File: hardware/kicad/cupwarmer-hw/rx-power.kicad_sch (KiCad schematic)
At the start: 41 parts, among them J1 I2C Service, J3 STATUS_MON, U1 STWLC38JRM

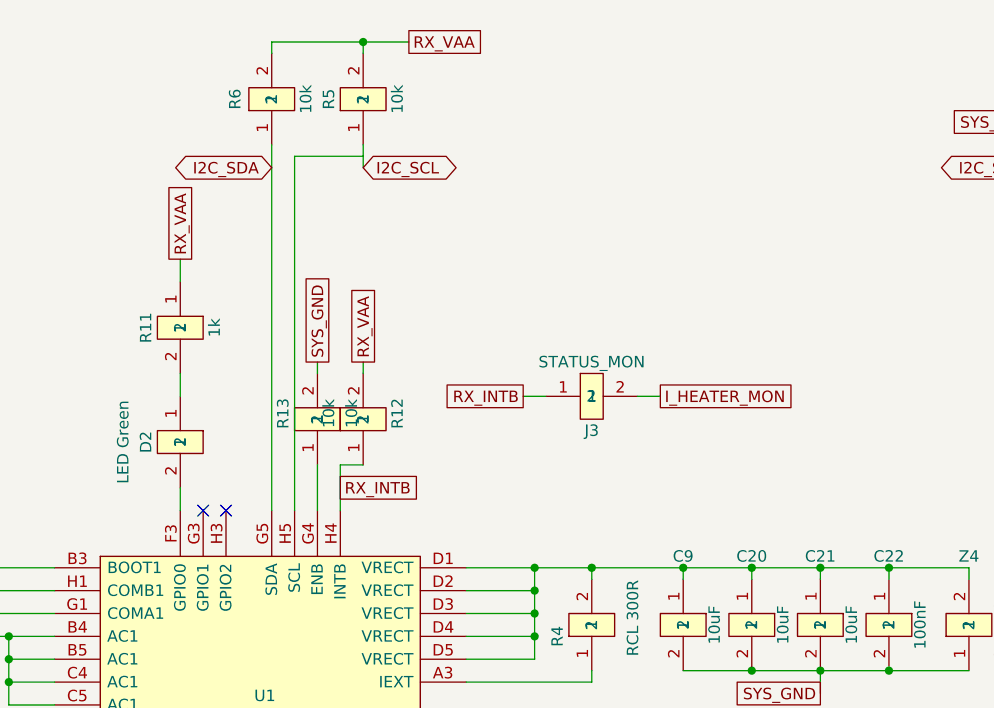
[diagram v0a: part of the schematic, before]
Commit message: Drop Cd (C15) parallel resonant cap
UM3154 §9.1.2 documents Cd as optional, used only for Qi-cert
backward compatibility with specific TX coils. cupwarmer is not
pursuing Qi certification, so the cap adds drift and loss without
benefit. Removed C15 (3.3 nF NP0 / Walsin 0603N332J500CT) from
the rx-power schematic, the PCB, and the BOM. Decision recorded
in docs/design-notes.md.

ERC clean; sch↔board parity unchanged otherwise.
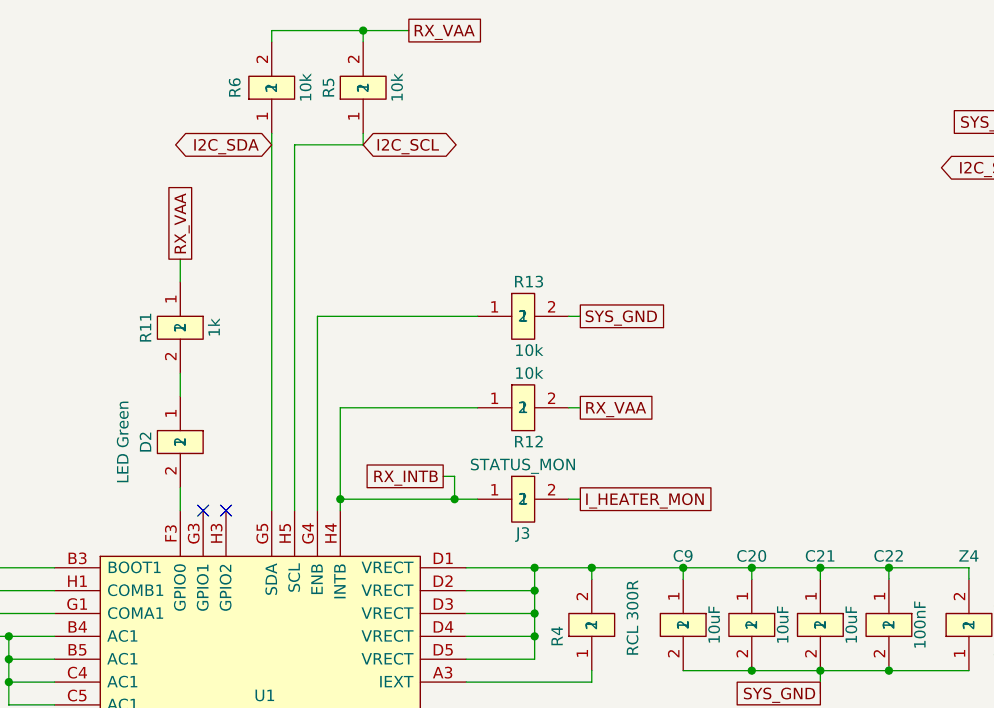
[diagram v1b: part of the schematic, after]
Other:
- moved on the sheet: J3, R12, R13, R5, R6

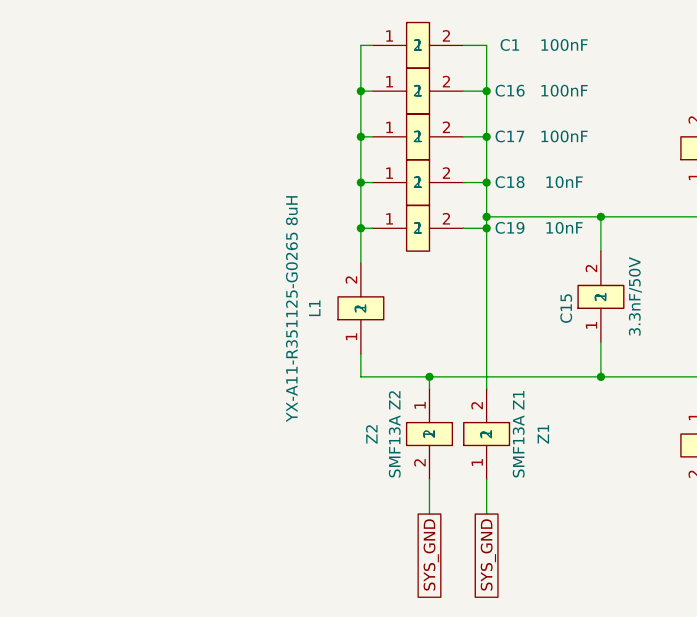
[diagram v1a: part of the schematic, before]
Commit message: Switch L1 footprint to Würth 760308102207 (P5.0mm)
Custom SolderWire footprint with 5.0mm pitch and φ1.2mm holes
matching the WE-WPCC 760308102207 lead pattern. Includes a
40×40mm rounded-square outline on Dwgs.User as a placement guide
for the coil module body. Schematic L1 properties (Value, MPN,
Manufacturer, LCSC, Footprint) updated to match the BOM.

ERC clean; PCB parity unchanged; no new DRC violations on L1.
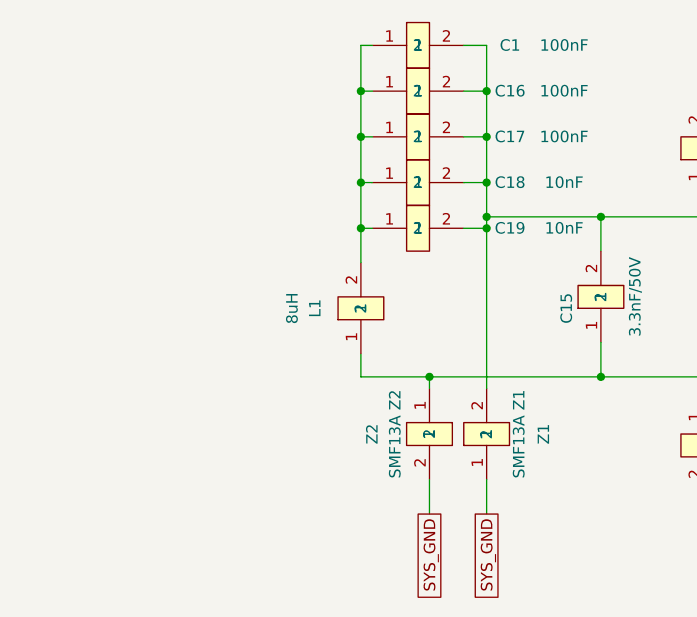
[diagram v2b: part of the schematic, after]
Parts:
- L1: value YX-A11-R351125-G0265 8uH -> 8uH; footprint Connector_Wire:SolderWire-0.5sqmm_1x02_P4.8mm_D0.9mm_OD2.3mm -> cupwarmer:SolderWire-Wuerth760308_1x02_P5.0mm_D1.2mm; LCSC C49297385 -> (none); MPN YX-A11-R351125-G0265 -> 760308102207; Manufacturer CND-tek -> Wuerth Elektronik
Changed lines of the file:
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@@
 			)
 		)
-		(property "Value" "YX-A11-R351125-G0265 8uH"
+		(property "Value" "8uH"
 			(at 50.8 105.41 0)
 			(show_name no)
@@
 			)
 		)
-		(property "Footprint" "Connector_Wire:SolderWire-0.5sqmm_1x02_P4.8mm_D0.9mm_OD2.3mm"
+		(property "Footprint" "cupwarmer:SolderWire-Wuerth760308_1x02_P5.0mm_D1.2mm"
 			(at 58.42 105.41 0)
 			(hide yes)
@@
 			)
 		)
-		(property "Manufacturer" "CND-tek"
+		(property "Manufacturer" "Wuerth Elektronik"
 			(at 0 0 0)
 			(hide yes)
@@
 			)
 		)
-		(property "LCSC" "C49297385"
+		(property "LCSC" ""
 			(at 0 0 0)
 			(hide yes)
@@
 			)
 		)
-		(property "MPN" "YX-A11-R351125-G0265"
+		(property "MPN" "760308102207"
 			(at 0 0 0)
 			(hide yes)

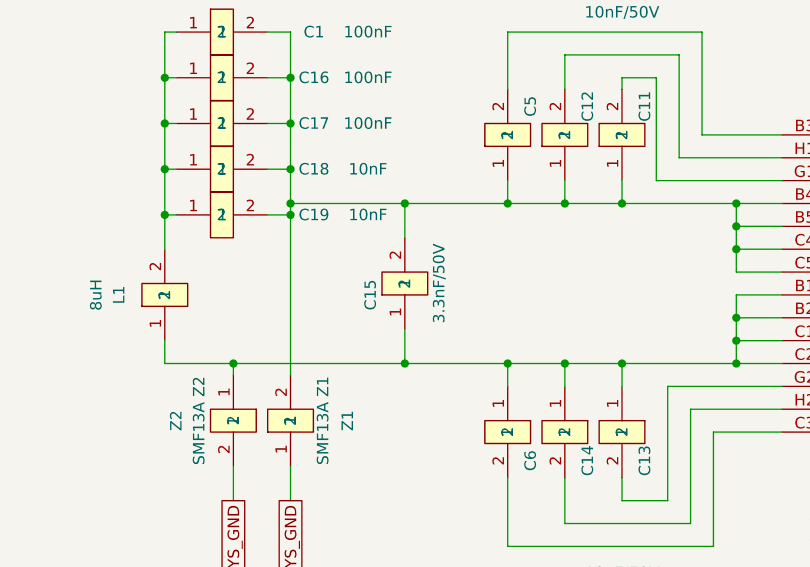
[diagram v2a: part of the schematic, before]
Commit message: Actually drop C15 (Cd) symbol + footprint
Earlier 522ecc1 commit removed the BOM row but the kicad-tool
delete on the schematic silently no-op'd, leaving C15 in
rx-power.kicad_sch and the PCB. This commit deletes the symbol,
its two dangling wire stubs, and the footprint. ERC clean.
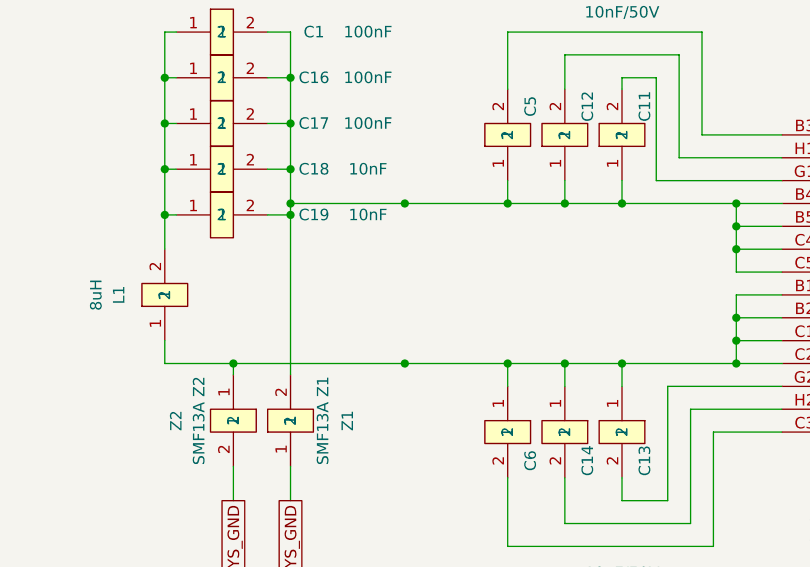
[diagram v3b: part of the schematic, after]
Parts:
- removed C15: 3.3nF/50V, Capacitor_SMD:C_0603_1608Metric, symbol cupwarmer:PASSIVE_2
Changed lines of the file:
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@@
-	(wire
-		(pts
-			(xy 85.09 95.25) (xy 85.09 99.06)
-		)
-		(stroke
-			(width 0)
-			(type default)
-		)
-	)
 	(wire
 		(pts
@@
 			(width 0)
 			(type solid)
-		)
-	)
-	(wire
-		(pts
-			(xy 85.09 109.22) (xy 85.09 113.03)
-		)
-		(stroke
-			(width 0)
-			(type default)
 		)
 	)
@@
 					(unit 1)
 				)
-			)
-		)
-	)
-	(symbol
-		(lib_id "cupwarmer:PASSIVE_2")
-		(at 85.09 104.14 90)
-		(unit 1)
-		(body_style 1)
-		(exclude_from_sim no)
-		(in_bom yes)
-		(on_board yes)
-		(in_pos_files yes)
-		(dnp no)
-		(property "Reference" "C15"
-			(at 81.28 105.41 0)
-			(show_name no)
-			(do_not_autoplace no)
-			(effects
-				(font
-					(size 1.27 1.27)
-				)
-			)
-		)
-		(property "Value" "3.3nF/50V"
-			(at 88.9 104.14 0)
-			(show_name no)
-			(do_not_autoplace no)
-			(effects
-				(font
-					(size 1.27 1.27)
-				)
-			)
-		)
-		(property "Footprint" "Capacitor_SMD:C_0603_1608Metric"
-			(at 85.09 104.14 0)
-			(hide yes)
-			(show_name no)
-			(do_not_autoplace no)
-			(effects
-				(font
-					(size 1.27 1.27)
-				)
-			)
-		)
-		(property "Datasheet" "~"
-			(at 85.09 104.14 0)
-			(hide yes)
-			(show_name no)
-			(do_not_autoplace no)
-			(effects
-				(font
-					(size 1.27 1.27)
-				)
-			)
-		)
-		(property "Description" "Resonant capacitor Cd (parallel)"
-			(at 85.09 104.14 0)
-			(hide yes)
-			(show_name no)
-			(do_not_autoplace no)
-			(effects
-				(font
-					(size 1.27 1.27)
-				)
-			)
-		)
-		(property "Manufacturer" "Walsin"
-			(at 0 0 0)
-			(hide yes)
-			(show_name no)
-			(do_not_autoplace no)
-			(effects
-				(font
-					(size 1.27 1.27)
-				)
-			)
-		)
-		(property "LCSC" "C152910"
-			(at 0 0 0)
-			(hide yes)
-			(show_name no)
-			(do_not_autoplace no)
-			(effects
-				(font
-					(size 1.27 1.27)
-				)
-			)
-		)
-		(property "MPN" "0603N332J500CT"
-			(at 0 0 0)
-			(hide yes)
-			(show_name no)
-			(do_not_autoplace no)
-			(effects
-				(font
-					(size 1.27 1.27)
-				)
-			)
-		)
-		(pin "1"
-		)
-		(pin "2"
-		)
-		(instances
-			(project "rx-power"
-				(path "/11111111-aaaa-bbbb-cccc-111111111111"
-					(reference "C15")
-					(unit 1)
-				)
-			)
-			(project "cupwarmer-hw"
-				(path "/f3c63676-f392-4700-9f58-a6787e1eb284/11111111-1111-1111-1111-111111111111"
-					(reference "C15")
-					(unit 1)
-				)
